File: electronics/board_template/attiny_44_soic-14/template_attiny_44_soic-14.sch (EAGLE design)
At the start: 17 parts, among them IC1 ATTINY441-SSU, IC3 NCP1117ST50T3G, J1 GROVE_CONNECTOR2.0_1X4, J2 GROVE_CONNECTOR2.0_1X4, J3 10129383-906001ALF, Y1 X322516MLB4SI

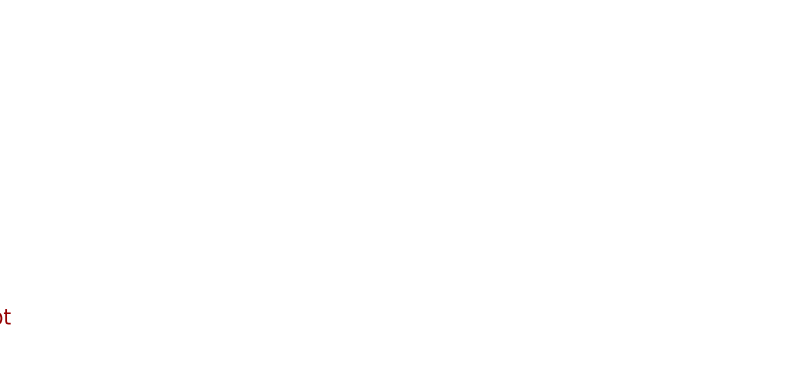
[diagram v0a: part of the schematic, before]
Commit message: Fiducials eingefügt
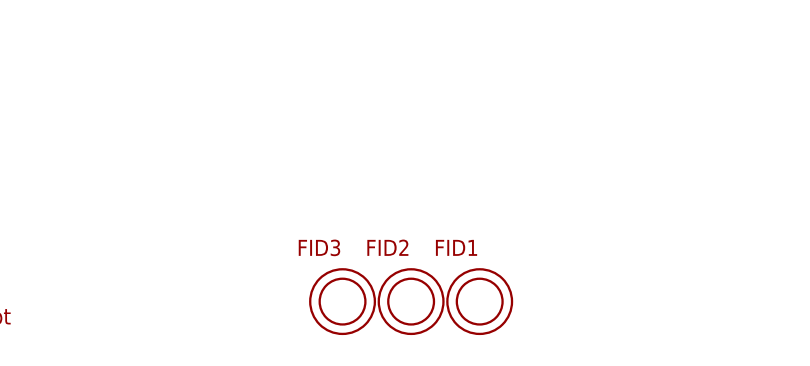
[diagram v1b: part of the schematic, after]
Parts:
- added FID1, FID2, FID3: OPEN-PNP-FIDUCIAL, topo-eng:OPEN-PNP-FIDUCIAL
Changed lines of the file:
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@@
 <part name="U$1" library="topo-eng" library_urn="urn:adsk.eagle:library:6646478" deviceset="LOGO_MORPHBOT" device="5MM"/>
 <part name="IC1" library="samacsys" deviceset="ATTINY441-SSU" device=""/>
+<part name="FID1" library="topo-eng" library_urn="urn:adsk.eagle:library:6646478" deviceset="OPEN-PNP-FIDUCIAL" device=""/>
+<part name="FID2" library="topo-eng" library_urn="urn:adsk.eagle:library:6646478" deviceset="OPEN-PNP-FIDUCIAL" device=""/>
+<part name="FID3" library="topo-eng" library_urn="urn:adsk.eagle:library:6646478" deviceset="OPEN-PNP-FIDUCIAL" device=""/>
 </parts>
 <sheets>
@@
 <attribute name="VALUE" x="212.09" y="144.78" size="1.778" layer="96" align="center-left"/>
 </instance>
+<instance part="FID1" gate="FID$1" x="157.48" y="5.08" smashed="yes">
+<attribute name="NAME" x="152.4" y="10.16" size="1.778" layer="94"/>
+</instance>
+<instance part="FID2" gate="FID$1" x="149.86" y="5.08" smashed="yes">
+<attribute name="NAME" x="144.78" y="10.16" size="1.778" layer="94"/>
+</instance>
+<instance part="FID3" gate="FID$1" x="142.24" y="5.08" smashed="yes">
+<attribute name="NAME" x="137.16" y="10.16" size="1.778" layer="94"/>
+</instance>
 </instances>
